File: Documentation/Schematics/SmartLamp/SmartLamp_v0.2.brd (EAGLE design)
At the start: 78.4 x 50.8 mm, 26 parts, among them IC1 DS3231/SO, J1 POWER_JACKPTH_BREAD, Q1 IRF1404, Q2 IRF1404, Q3 IRF1404, U1 HM-10

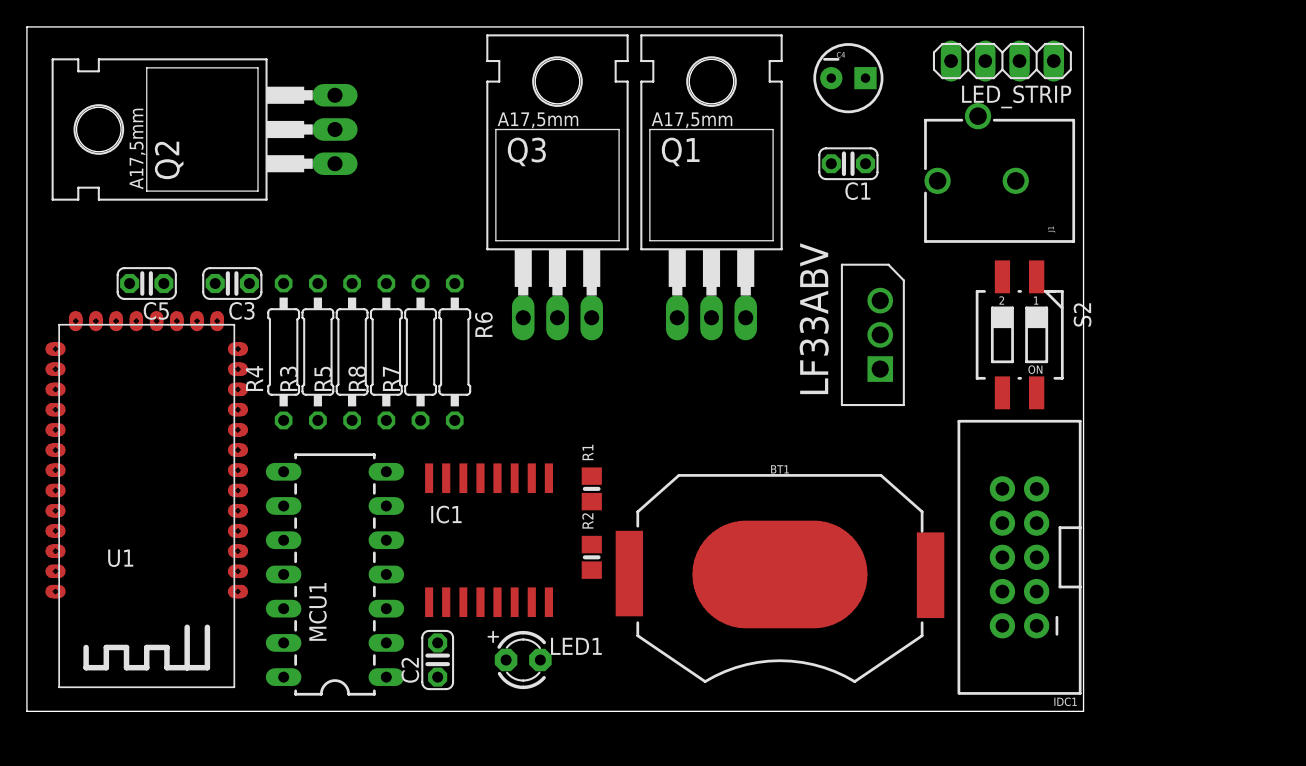
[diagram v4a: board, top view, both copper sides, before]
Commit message: Revisited board, ERC on schematic
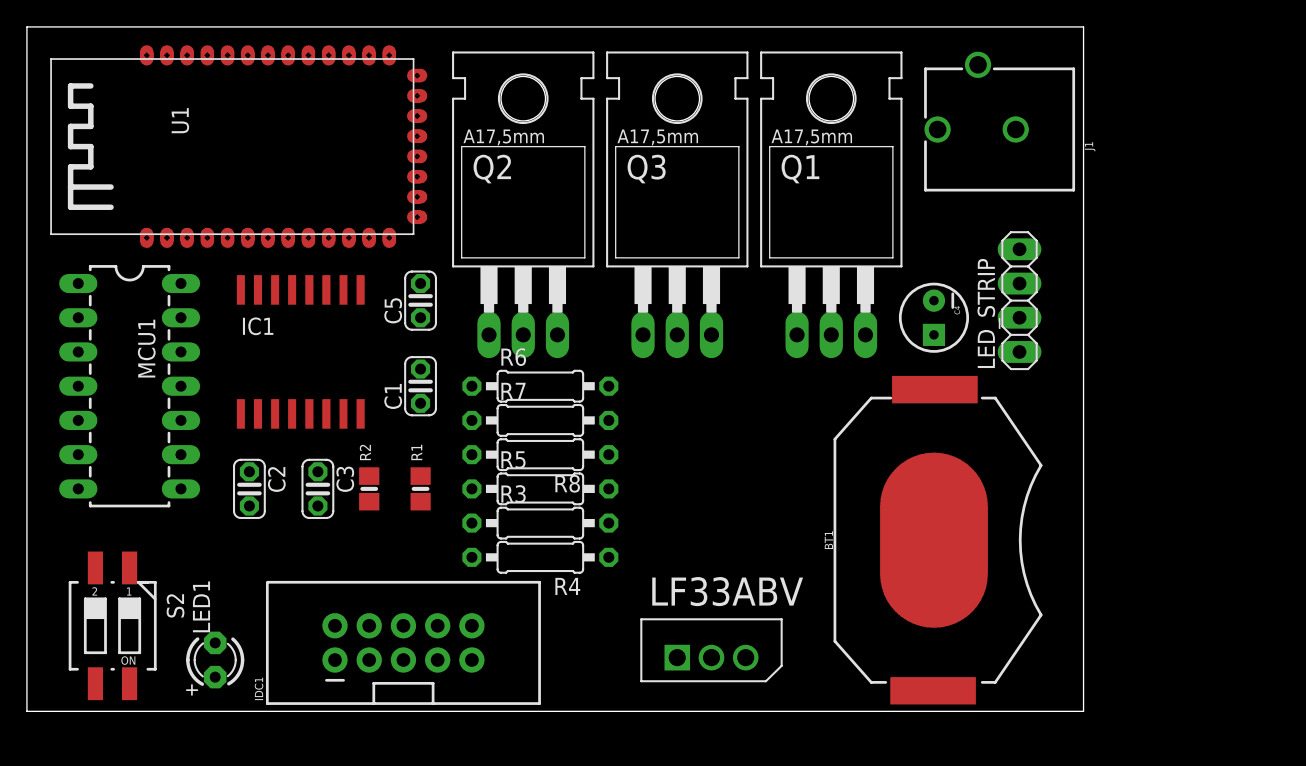
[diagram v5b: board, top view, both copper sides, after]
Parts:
- BT1: value (none) -> BT1
- IDC1: value (none) -> IDC1
- moved S2 70.7 mm to (6.35, 6.35)
- moved IDC1 46.2 mm to (27.9, 5.08), turned to 90 degrees
- moved C1 35.8 mm to (29.2, 24.1), turned to 90 degrees
- moved U1 27.4 mm to (15.2, 41.9), turned to 90 degrees
- moved LF33ABV 26.9 mm to (53.3, 5.08), turned to 0 degrees
- moved R4 24.4 mm to (38.1, 11.4), turned to 180 degrees
- moved LED1 22.9 mm to (14.0, 3.81), turned to 90 degrees
- moved Q2 22.2 mm to (36.8, 34.3), turned to 0 degrees
- moved R3 20.8 mm to (38.1, 14.0), turned to 0 degrees
- moved C5 20.4 mm to (29.2, 30.5), turned to 90 degrees
- moved IC1 19.8 mm to (20.3, 26.7)
- moved MCU1 19.0 mm to (7.62, 22.9), turned to 270 degrees
- moved C2 18.9 mm to (16.5, 16.5), turned to 270 degrees
- moved C4 18.9 mm to (67.3, 29.2), turned to 270 degrees
- moved LED_STRIP 17.8 mm to (73.7, 30.5), turned to 90 degrees
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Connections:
- removed net !RTC_RST: IC1.4
- removed net 3.3V: C1.1, C2.1, C3.1, C4.1, IC1.2, IDC1.2, LF33ABV.3, MCU1.1, R1.1, R2.1, R6.1, R7.1, S2.1
- removed net N$5: BT1.NEGATIVE, IC1.14
- new net +3V3: C1.1, C3.1, C4.1, IC1.2, LF33ABV.3, R1.1, R2.1, R6.1, R7.1, S2.1
- new net 3V3: C2.1, IDC1.2, MCU1.1
- new net VBAT: BT1.POSITIVE@1, BT1.POSITIVE@2, BT1.POSITIVE@3, BT1.POSITIVE@4, IC1.14
- net GND: now also BT1.NEGATIVE; no longer BT1.POSITIVE@1, BT1.POSITIVE@2, BT1.POSITIVE@3, BT1.POSITIVE@4
